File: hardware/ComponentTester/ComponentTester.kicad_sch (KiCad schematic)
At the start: 18 parts, among them J1 Conn_01x06_Socket, J2 AVR-ISP-6, J3 Conn_02x07_Counter_Clockwise, J4 GameBoy_GamePak_DMG-09, J5 Conn_01x03_Pin, SW1 SW_Push, U1 ATmega328P-A

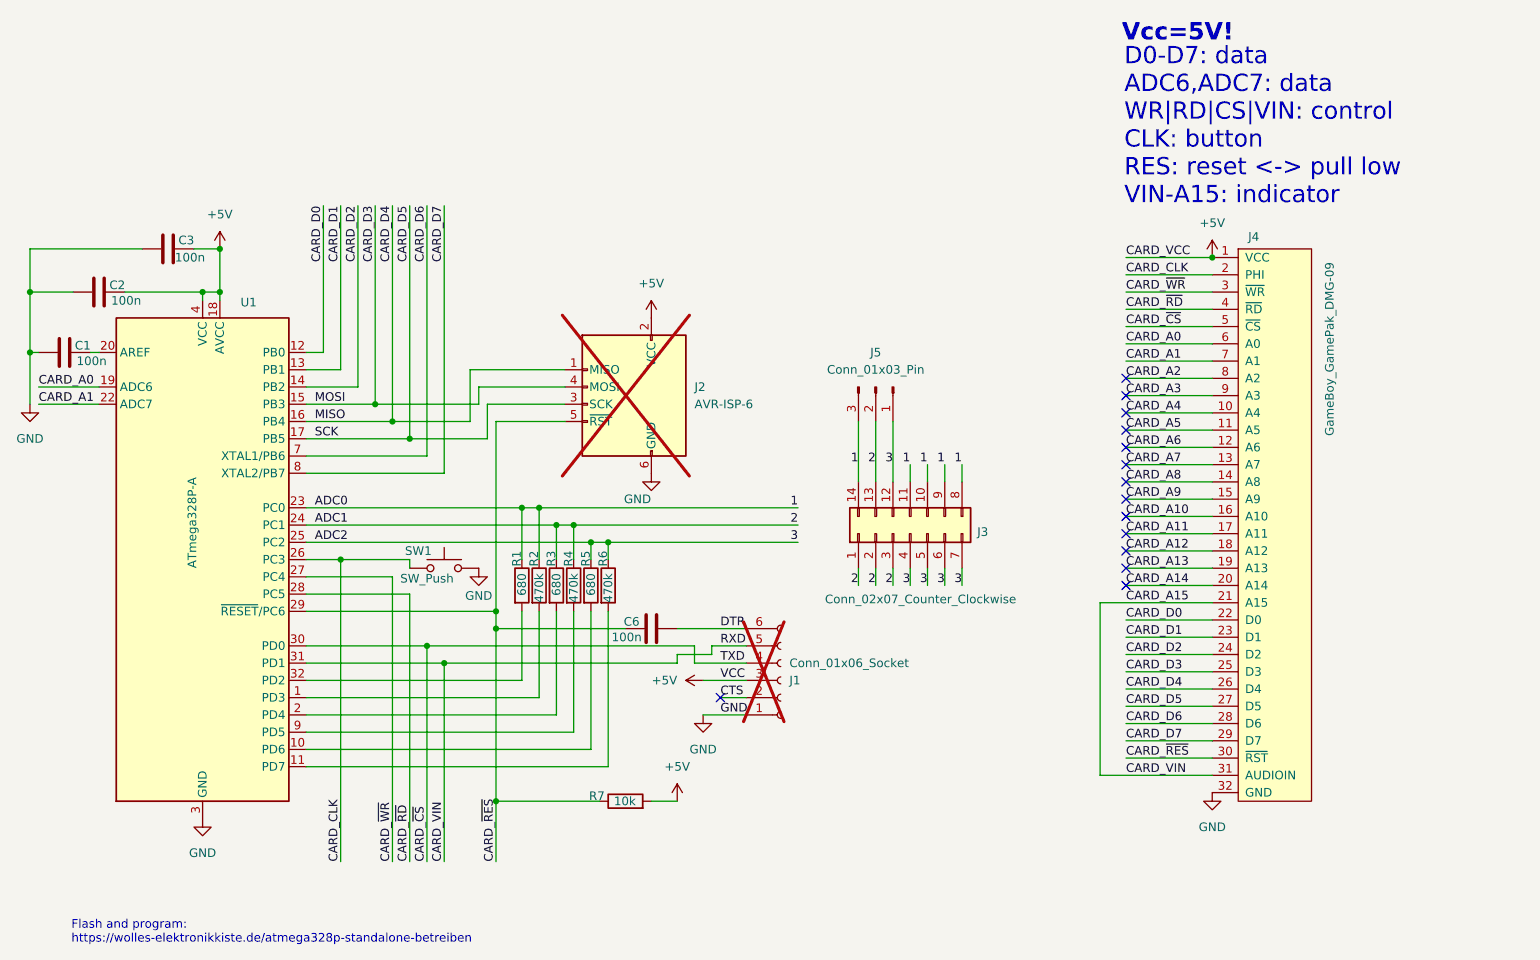
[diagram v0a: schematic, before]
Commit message: replace ATmega328P with ATmegaPB
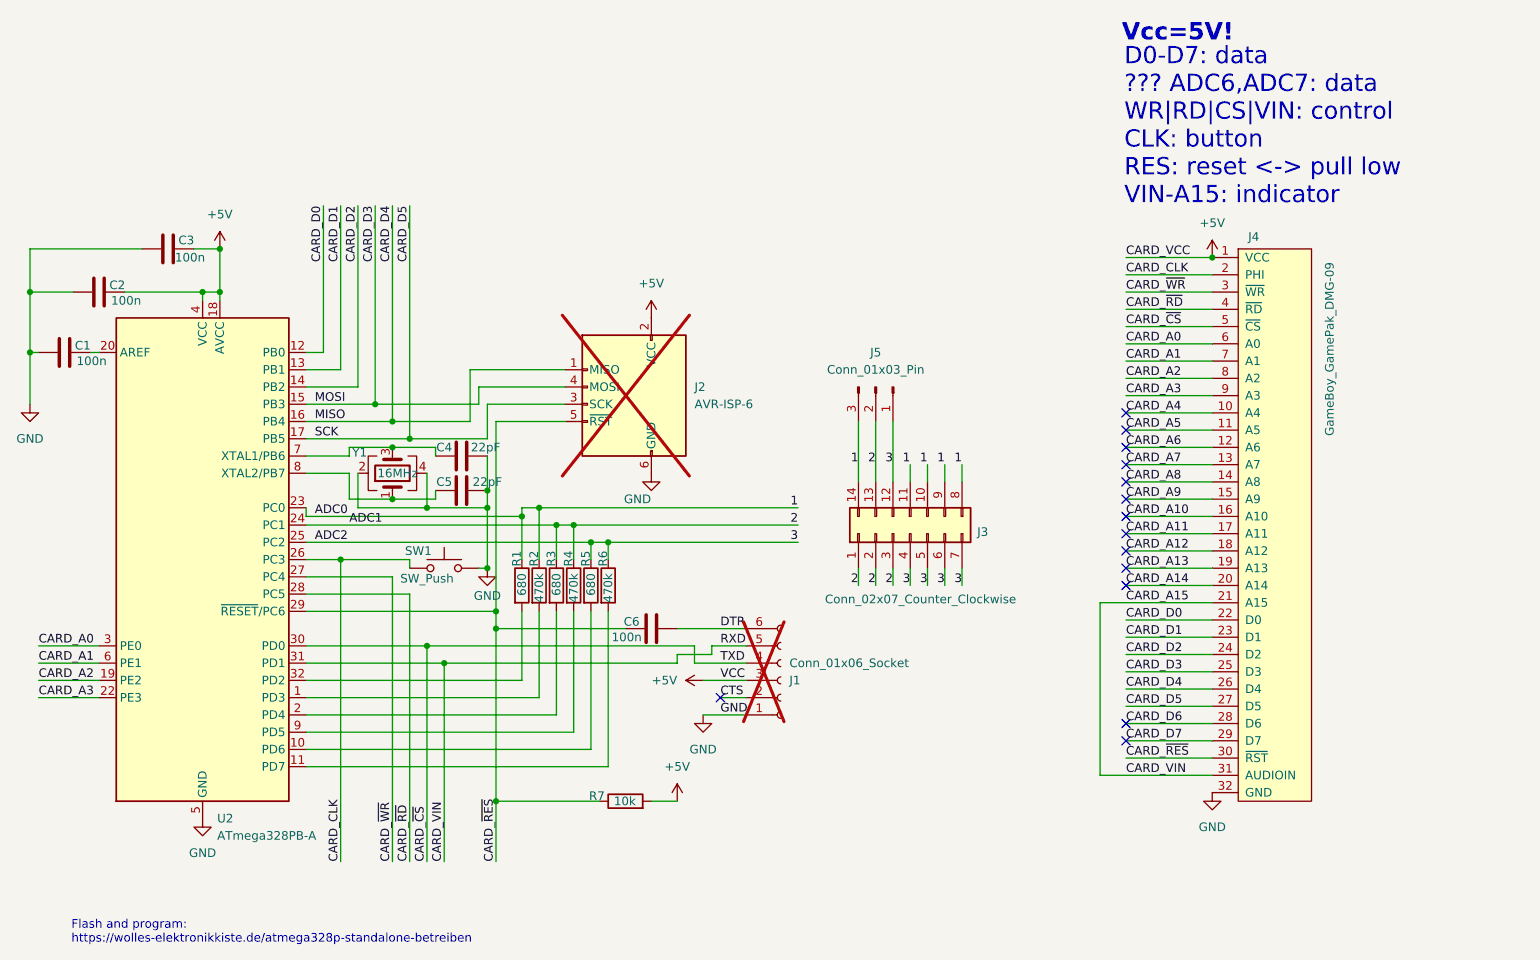
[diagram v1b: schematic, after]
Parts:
- removed U1: ATmega328P-A, Package_QFP:TQFP-32_7x7mm_P0.8mm, symbol MCU_Microchip_ATmega:ATmega328P-A
- added C4, C5: 22pF, Capacitor_SMD:C_0805_2012Metric_Pad1.18x1.45mm_HandSolder, symbol Device:C
- added U2: ATmega328PB-A, Package_QFP:TQFP-32_7x7mm_P0.8mm, symbol MCU_Microchip_ATmega:ATmega328PB-A
- added Y1: 16MHz, Crystal:Crystal_SMD_3225-4Pin_3.2x2.5mm, symbol Device:Crystal_GND24
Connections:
- net +5V: now also U2.18 (AVCC), U2.4 (VCC)
- net 1: now also U2.23 (PC0)
- net 2: now also U2.24 (PC1)
- net 3: now also U2.25 (PC2)
- net CARD_A0: now also U2.3 (PE0)
- net CARD_A1: now also U2.6 (PE1)
- net CARD_A15: now also U2.31 (PD1)
- net CARD_A2: now also U2.19 (PE2)
- net CARD_A3: now also U2.22 (PE3)
- net CARD_CLK: now also U2.26 (PC3)
- net CARD_D0: now also U2.12 (PB0)
- net CARD_D1: now also U2.13 (PB1)
- net CARD_D2: now also U2.14 (PB2)
- net CARD_D3: now also U2.15 (PB3)
- net CARD_D4: now also U2.16 (PB4)
- net CARD_D5: now also U2.17 (PB5)
- net CARD_~{CS}: now also U2.30 (PD0)
- net CARD_~{RD}: now also U2.28 (PC5)
- net CARD_~{RES}: now also U2.29 (~{RESET}/PC6)
- net CARD_~{WR}: now also U2.27 (PC4)
- net GND: now also C4.2, C5.2, U2.21 (GND), U2.5 (GND), Y1.2, Y1.4
- net at R1.2: now also U2.32 (PD2)
- net at C1.1: now also U2.20 (AREF)
- net at R3.2: now also U2.2 (PD4)
- net at R4.2: now also U2.9 (PD5)
- net at R2.2: now also U2.1 (PD3)
- net at R5.2: now also U2.10 (PD6)
- net at R6.2: now also U2.11 (PD7)
- new net: C5.1, U2.8 (XTAL2/PB7), Y1.1
- new net: C4.1, U2.7 (XTAL1/PB6), Y1.3
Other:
- note added: "D0-D7: data ??? ADC6,ADC7: data WR|RD|CS|VIN: control CLK: button RES: reset <-> pull low VIN-A15: indicator"
- note removed: "D0-D7: data ADC6,ADC7: data WR|RD|CS|VIN: control CLK: button RES: reset <-> pull low VIN-A15: indicator"
